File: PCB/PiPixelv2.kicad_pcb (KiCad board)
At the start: 2 copper layers, 65 x 30 mm, 13 parts, among them CON1 BARREL_JACK, J1 RPi_GPIO, P1 CONN_01X04, P2 CONN_01X02, U1 74AHC125

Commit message: Further PCB changes, library adds
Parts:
- removed ? (x4): , RPi_Hat:RPi_Hat_Mounting_Hole
- removed CON1: BARREL_JACK, APM_BarrelJack:ML_BARREL_JACK_ROUND_PADS_SHORT
- removed P1: CONN_01X04, w_conn_mpt:mpt_0,5%2f4-2,54
- removed P2: CONN_01X02, w_conn_mkds:mkds_1,5-2
- added H1: 3mm_Mounting_Hole, RPi_HAT_MountingHole:NPTH_3mm_ID, F.Cu at (16.0, 28.0)
- added H1: 3mm_Mounting_Hole, RPi_HAT_MountingHole:NPTH_3mm_ID, F.Cu at (16.0, 51.0)
- added H1: 3mm_Mounting_Hole, RPi_HAT_MountingHole:NPTH_3mm_ID, F.Cu at (74.0, 51.0)
- added H1: 3mm_Mounting_Hole, RPi_HAT_MountingHole:NPTH_3mm_ID, F.Cu at (74.0, 28.0)
- added J2: Barrel_Jack_Switch, APM_BarrelJack:ML_BARREL_JACK_ROUND_PADS_SHORT, F.Cu at (15.5, 37.5)
- added J3: Conn_01x02, w_conn_mkds:mkds_1,5-2, F.Cu at (27.9, 47.6)
- added J4: Conn_01x04, w_conn_mpt:mpt_0,5%2f4-2,54, F.Cu at (72.0, 39.0)
- J1: value RPi_GPIO -> Raspberry_Pi_2_3; footprint RPi_Hat:Pin_Header_Straight_2x20 -> Pin_Headers:Pin_Header_Straight_2x20_Pitch2.54mm
- JP1: value Jumper_NC_Small -> SolderJumper_2_Bridged; footprint Custom:small_jump -> Jumper:SolderJumper-2_P1.3mm_Bridged_Pad1.0x1.5mm
- JP2: value Jumper_NO_Small -> SolderJumper_3_Open; footprint Custom:small_jump -> Jumper:SolderJumper-3_P1.3mm_Open_Pad1.0x1.5mm_NumberLabels
- JP3: value Jumper_NO_Small -> SolderJumper_2_Open; footprint Custom:small_jump -> Jumper:SolderJumper-2_P1.3mm_Open_Pad1.0x1.5mm
- U1: footprint Custom:DIP_14 -> SMD_Packages:SOIC-14_N
- moved J1 24.0 mm to (21.0, 29.5)
- moved G*** 10.2 mm to (38.4, 43.1)
- moved JP3 9.66 mm to (31.0, 35.0), turned to 0 degrees
- moved JP2 5.35 mm to (48.2, 37.4)
- moved U1 4.69 mm to (60.3, 34.0)
- moved JP1 2.28 mm to (45.1, 37.8)
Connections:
- JP1 pad 2: Net-(JP1-Pad2) -> LS_IN
- JP2 pad 2: Net-(JP1-Pad2) -> LS_IN
- JP3 pad 1: PWM_13 -> PWR
- JP3 pad 2: Net-(JP1-Pad2) -> 5V
- U1 pad 2: Net-(JP1-Pad2) -> LS_IN
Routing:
- net GND: track 183.2 -> 0.00 mm, vias 2 -> 0
- net 5V: track 75.4 -> 0.00 mm, vias 2 -> 0
- net PWR: track 70.2 -> 0.00 mm
- net Net-(J4-Pad2): track 32.3 -> 0.00 mm
- net PWM_13: track 24.9 -> 0.00 mm, vias 2 -> 0
- net CLK: track 24.3 -> 0.00 mm
- net Net-(J4-Pad3): track 22.0 -> 0.00 mm
- net PWM_18: track 16.2 -> 0.00 mm, vias 2 -> 0
- net Net-(JP1-Pad2): track 15.2 -> 0.00 mm
- net MOSI: track 7.11 -> 0.00 mm
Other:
- board text removed: "Data Pin Select"
- board text removed: "GP13"
- board text removed: "GP18"
- board text removed: "SPI_DAT"

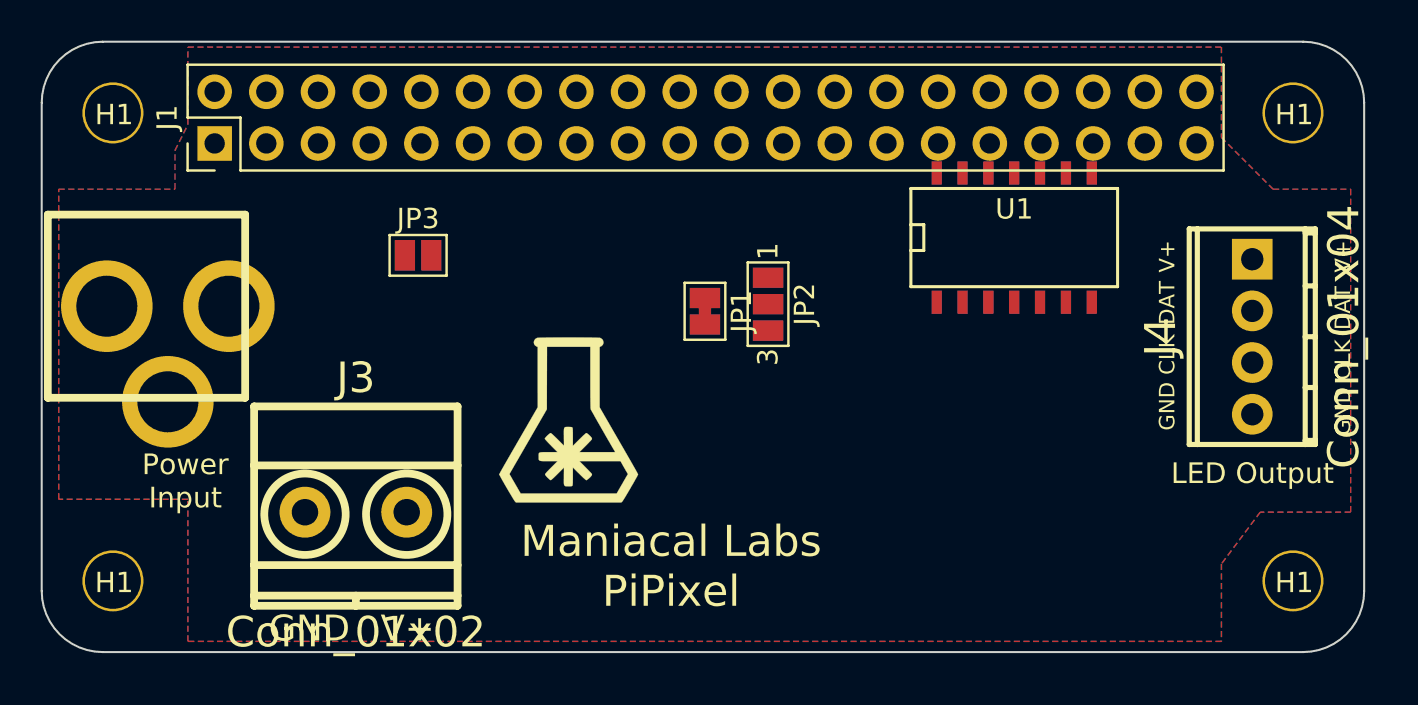
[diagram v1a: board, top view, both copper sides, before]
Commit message: v2 PCB layout, traces complete.
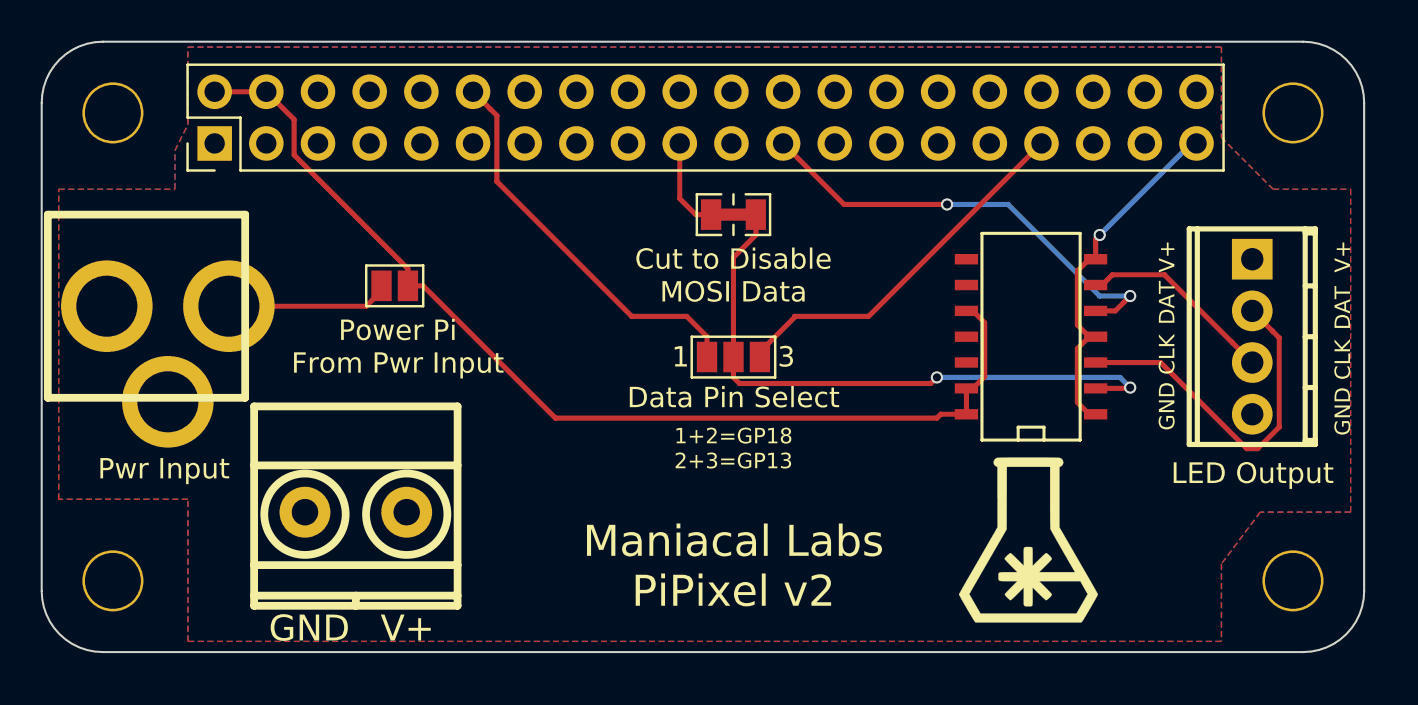
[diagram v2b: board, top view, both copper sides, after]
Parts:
- JP1: footprint Jumper:SolderJumper-2_P1.3mm_Bridged_Pad1.0x1.5mm -> CuttableSolderJumper:SolderJumper-2_P1.3mm_Bridged_Pad1.0x1.5mm
- moved G*** 23.4 mm to (61.0, 49.0)
- moved U1 5.05 mm to (61.0, 39.0), turned to 90 degrees
- moved JP1 4.95 mm to (46.5, 33.0), turned to 0 degrees
- moved JP2 3.11 mm to (46.5, 40.0), turned to 0 degrees
- moved JP3 1.89 mm to (29.9, 36.5)
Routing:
- net 5V: track 0.00 -> 51.4 mm
- net LS_IN: track 0.00 -> 30.1 mm, vias 0 -> 2
- net CLK: track 0.00 -> 22.2 mm, vias 0 -> 2
- net PWM_18: track 0.00 -> 19.4 mm
- net PWM_13: track 0.00 -> 18.4 mm
- net Net-(J4-Pad2): track 0.00 -> 17.5 mm
- net GND: track 0.00 -> 17.4 mm, vias 0 -> 1
- net Net-(J4-Pad3): track 0.00 -> 9.69 mm
- net PWR: track 0.00 -> 8.06 mm
- net MOSI: track 0.00 -> 4.58 mm
- added copper zone on B.Cu, net GND
- added copper zone on F.Cu, net PWR
- removed copper zone on F.Cu, net GND
- removed copper zone on B.Cu, net PWR
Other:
- board text added: "1+2=GP18 2+3=GP13"
- board text added: "Cut to Disable MOSI Data"
- board text added: "Data Pin Select"
- board text added: "Maniacal Labs PiPixel v2"
- board text added: "Power Pi From Pwr Input"
- board text added: "Pwr Input"
- board text removed: "Maniacal Labs PiPixel"
- board text removed: "Power Input"

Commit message: Made GND connections to top row of pins on Pi header, DRC Pass
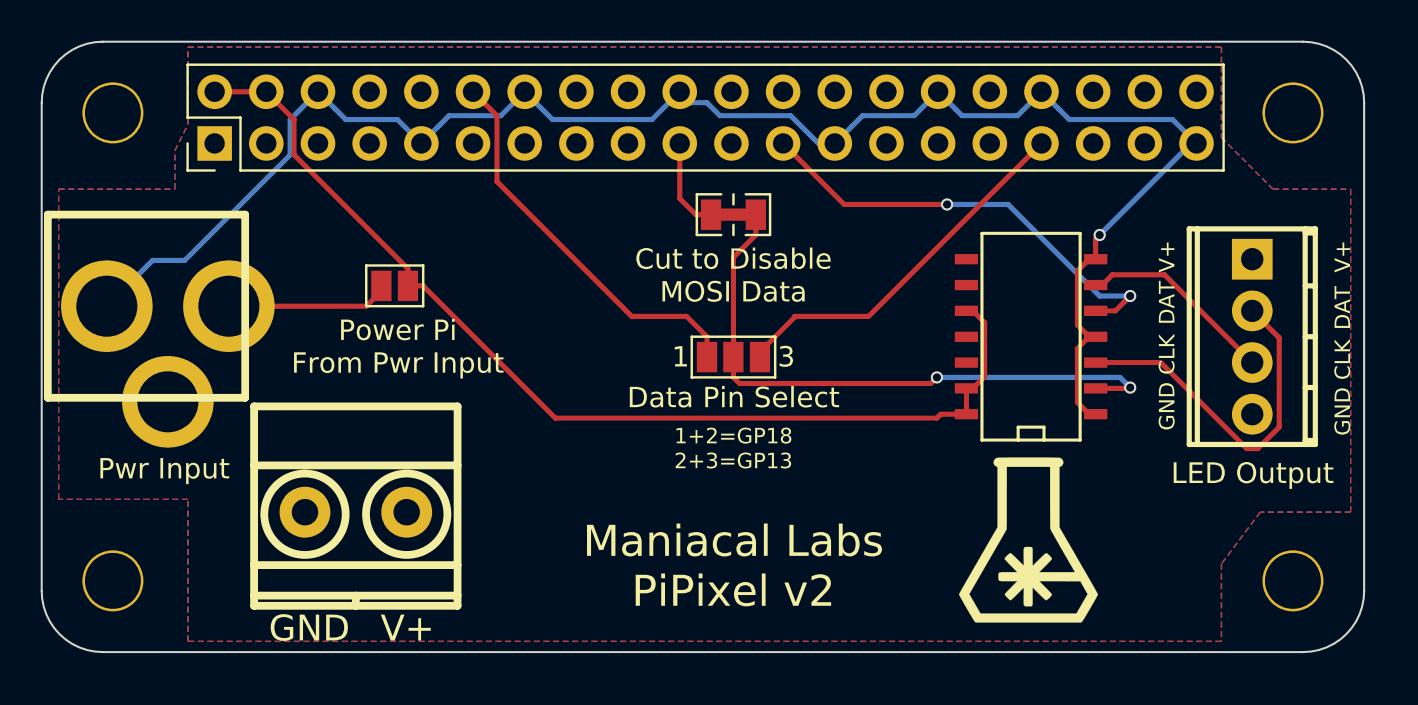
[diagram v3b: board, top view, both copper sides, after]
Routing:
- net GND: track 17.4 -> 83.7 mm
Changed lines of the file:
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@@
     (thickness 1.6)
     (drawings 25)
-    (tracks 87)
+    (tracks 122)
     (zones 0)
     (modules 13)
@@
   (segment (start 69 29.5) (end 69.26 29.5) (width 0.25) (layer B.Cu) (net 26))
   (segment (start 64.5 34) (end 69 29.5) (width 0.25) (layer B.Cu) (net 26))
+  (segment (start 62.489999 27.809999) (end 61.64 26.96) (width 0.25) (layer B.Cu) (net 26))
+  (segment (start 63.004999 28.324999) (end 62.489999 27.809999) (width 0.25) (layer B.Cu) (net 26))
+  (segment (start 68.084999 28.324999) (end 63.004999 28.324999) (width 0.25) (layer B.Cu) (net 26))
+  (segment (start 69.26 29.5) (end 68.084999 28.324999) (width 0.25) (layer B.Cu) (net 26))
+  (segment (start 37.089999 27.809999) (end 36.24 26.96) (width 0.25) (layer B.Cu) (net 26))
+  (segment (start 37.604999 28.324999) (end 37.089999 27.809999) (width 0.25) (layer B.Cu) (net 26))
+  (segment (start 42.495001 28.324999) (end 37.604999 28.324999) (width 0.25) (layer B.Cu) (net 26))
+  (segment (start 43.86 26.96) (end 42.495001 28.324999) (width 0.25) (layer B.Cu) (net 26))
+  (segment (start 32.009999 28.650001) (end 31.16 29.5) (width 0.25) (layer B.Cu) (net 26))
+  (segment (start 32.524999 28.135001) (end 32.009999 28.650001) (width 0.25) (layer B.Cu) (net 26))
+  (segment (start 35.064999 28.135001) (end 32.524999 28.135001) (width 0.25) (layer B.Cu) (net 26))
+  (segment (start 36.24 26.96) (end 35.064999 28.135001) (width 0.25) (layer B.Cu) (net 26))
+  (segment (start 26.929999 27.809999) (end 26.08 26.96) (width 0.25) (layer B.Cu) (net 26))
+  (segment (start 27.444999 28.324999) (end 26.929999 27.809999) (width 0.25) (layer B.Cu) (net 26))
+  (segment (start 29.984999 28.324999) (end 27.444999 28.324999) (width 0.25) (layer B.Cu) (net 26))
+  (segment (start 31.16 29.5) (end 29.984999 28.324999) (width 0.25) (layer B.Cu) (net 26))
+  (segment (start 57.409999 27.809999) (end 56.56 26.96) (width 0.25) (layer B.Cu) (net 26))
+  (segment (start 57.735001 28.135001) (end 57.409999 27.809999) (width 0.25) (layer B.Cu) (net 26))
+  (segment (start 60.464999 28.135001) (end 57.735001 28.135001) (width 0.25) (layer B.Cu) (net 26))
+  (segment (start 61.64 26.96) (end 60.464999 28.135001) (width 0.25) (layer B.Cu) (net 26))
+  (segment (start 52.329999 28.650001) (end 51.48 29.5) (width 0.25) (layer B.Cu) (net 26))
+  (segment (start 52.844999 28.135001) (end 52.329999 28.650001) (width 0.25) (layer B.Cu) (net 26))
+  (segment (start 55.384999 28.135001) (end 52.844999 28.135001) (width 0.25) (layer B.Cu) (net 26))
+  (segment (start 56.56 26.96) (end 55.384999 28.135001) (width 0.25) (layer B.Cu) (net 26))
+  (segment (start 44.4 27.5) (end 43.86 26.96) (width 0.25) (layer B.Cu) (net 26))
+  (segment (start 45.200998 27.5) (end 44.4 27.5) (width 0.25) (layer B.Cu) (net 26))
+  (segment (start 45.835999 28.135001) (end 45.200998 27.5) (width 0.25) (layer B.Cu) (net 26))
+  (segment (start 49.314003 28.135001) (end 45.835999 28.135001) (width 0.25) (layer B.Cu) (net 26))
+  (segment (start 51.48 29.5) (end 50.679002 29.5) (width 0.25) (layer B.Cu) (net 26))
+  (segment (start 50.679002 29.5) (end 49.314003 28.135001) (width 0.25) (layer B.Cu) (net 26))
+  (segment (start 17.950659 35.250001) (end 15.70066 37.5) (width 0.25) (layer B.Cu) (net 26))
+  (segment (start 19.529001 35.250001) (end 17.950659 35.250001) (width 0.25) (layer B.Cu) (net 26))
+  (segment (start 24.715001 30.064001) (end 19.529001 35.250001) (width 0.25) (layer B.Cu) (net 26))
+  (segment (start 24.715001 28.324999) (end 24.715001 30.064001) (width 0.25) (layer B.Cu) (net 26))
+  (segment (start 26.08 26.96) (end 24.715001 28.324999) (width 0.25) (layer B.Cu) (net 26))
   (segment (start 21 26.96) (end 23.54 26.96) (width 0.25) (layer F.Cu) (net 27))
   (segment (start 30.5 35.659002) (end 30.5 36.5) (width 0.25) (layer F.Cu) (net 27))
